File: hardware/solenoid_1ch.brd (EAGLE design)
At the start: 37.3 x 34 mm, 18 parts, among them U2 AP2204R

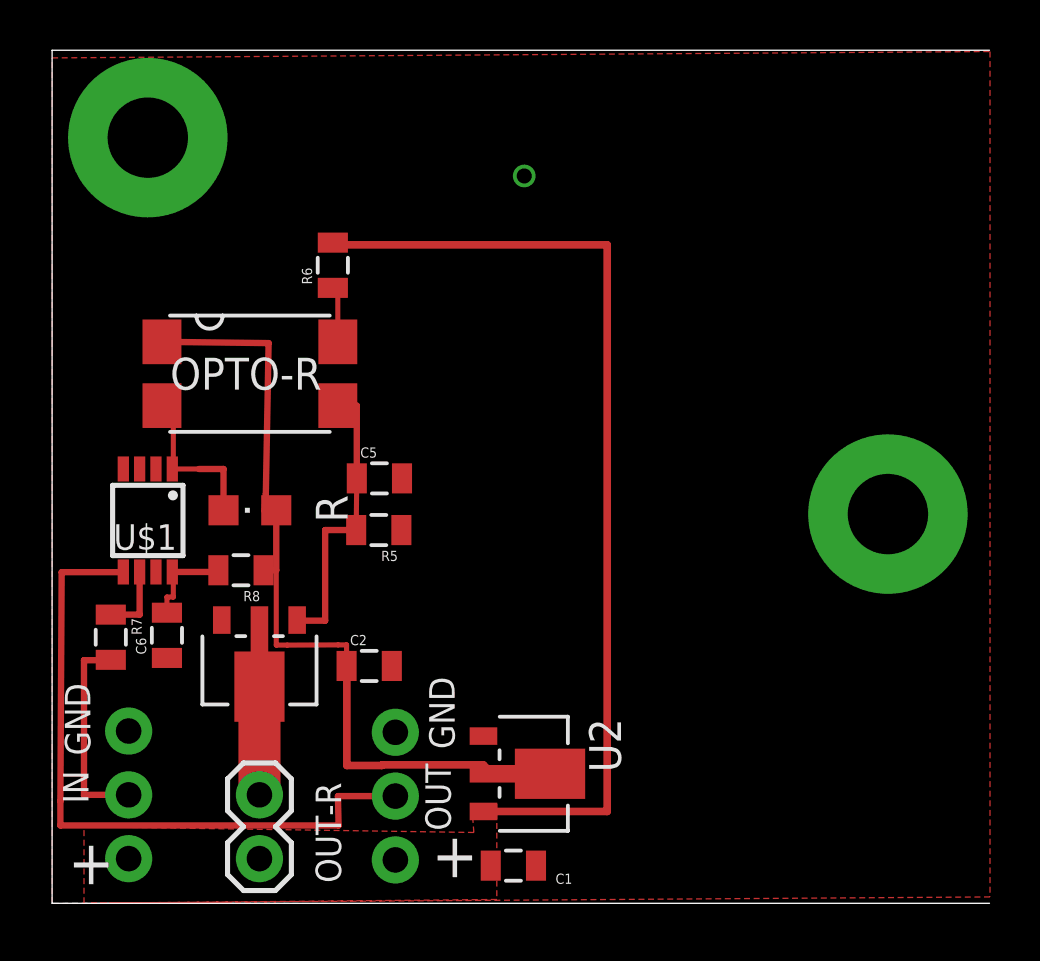
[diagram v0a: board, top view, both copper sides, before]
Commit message: Added protection diodes
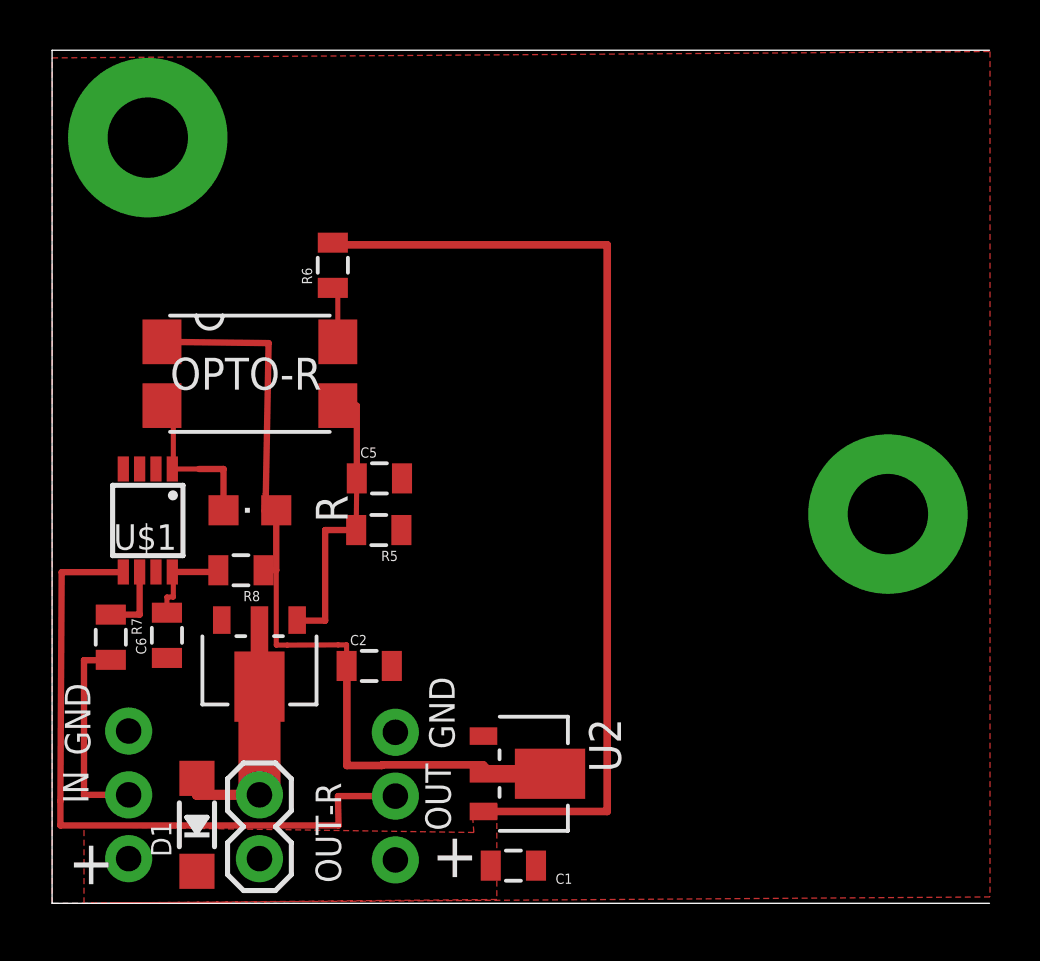
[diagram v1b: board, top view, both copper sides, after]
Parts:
- added D1: (no value), microbuilder:SOD-123
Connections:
- net N$12: now also D1.A
- net VDD: now also D1.C
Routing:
- net N$12: track 6.61 -> 9.75 mm
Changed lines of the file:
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@@
 <setting verticaltext="up"/>
 </settings>
-<grid distance="1" unitdist="mil" unit="mil" style="lines" multiple="1" display="yes" altdistance="0.001" altunitdist="inch" altunit="inch"/>
+<grid distance="1" unitdist="mil" unit="mm" style="lines" multiple="1" display="yes" altdistance="0.00254" altunitdist="mm" altunit="mm"/>
 <layers>
 <layer number="1" name="Top" color="4" fill="1" visible="yes" active="yes"/>
@@
 <element name="C6" library="SparkFun-Capacitors" package="0805" value=".1uf" x="4.572" y="10.668" rot="R90"/>
 <element name="R8" library="SparkFun-Passives" package="0805" value="100" x="7.5184" y="13.2588" rot="R180"/>
+<element name="D1" library="microbuilder" package="SOD-123" value="" x="5.7658" y="3.1242" rot="R90"/>
 </elements>
 <signals>
@@
 <wire x1="22.098" y1="26.2128" x2="11.176" y2="26.2128" width="0.3048" layer="1"/>
 <wire x1="11.176" y1="26.2128" x2="11.176" y2="26.3" width="0.3048" layer="1"/>
+<contactref element="D1" pad="C"/>
 </signal>
 <signal name="VCC">
@@
 <wire x1="8.255" y1="8.625" x2="8.255" y2="4.318" width="1.6764" layer="1"/>
 <wire x1="8.255" y1="10.925" x2="8.255" y2="8.625" width="0.4064" layer="1"/>
+<contactref element="D1" pad="A"/>
+<wire x1="8.255" y1="4.318" x2="5.7658" y2="4.318" width="0.4064" layer="1"/>
+<wire x1="5.7658" y1="4.318" x2="5.7658" y2="4.9742" width="0.4064" layer="1"/>
 </signal>
 <signal name="N$13">
@@
 <wire x1="0.3302" y1="4.064" x2="0.3302" y2="3.0988" width="0.254" layer="1"/>
 </signal>
-<signal name="N$17">
-<via x="18.796" y="28.956" extent="1-16" drill="0.6"/>
-</signal>
 <signal name="N$30">
